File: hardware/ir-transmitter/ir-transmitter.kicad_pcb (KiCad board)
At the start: 2 copper layers, 50 x 20 mm, 16 parts, among them T1 Q_NMOS_GSD, T2 Q_NMOS_GSD, X1 Conn_01x05

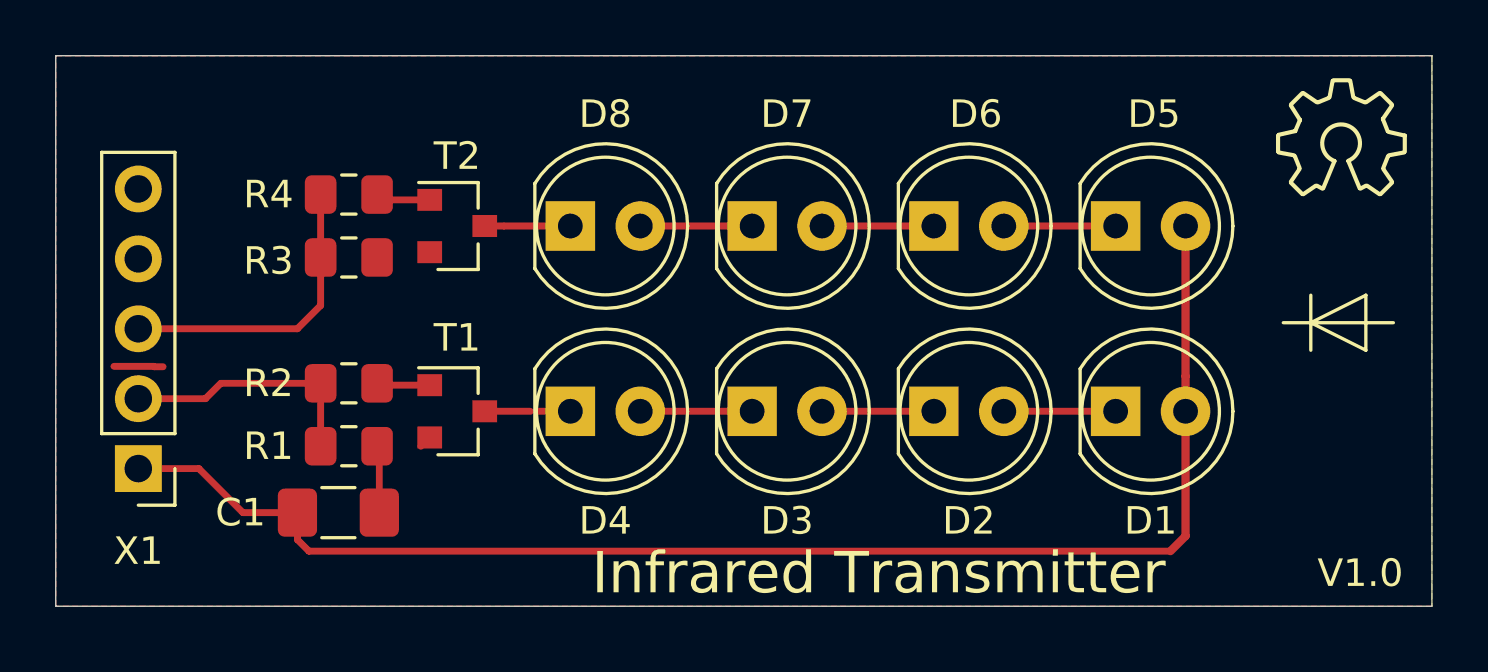
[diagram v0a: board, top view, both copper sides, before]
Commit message: Make receiver PCB two-sided
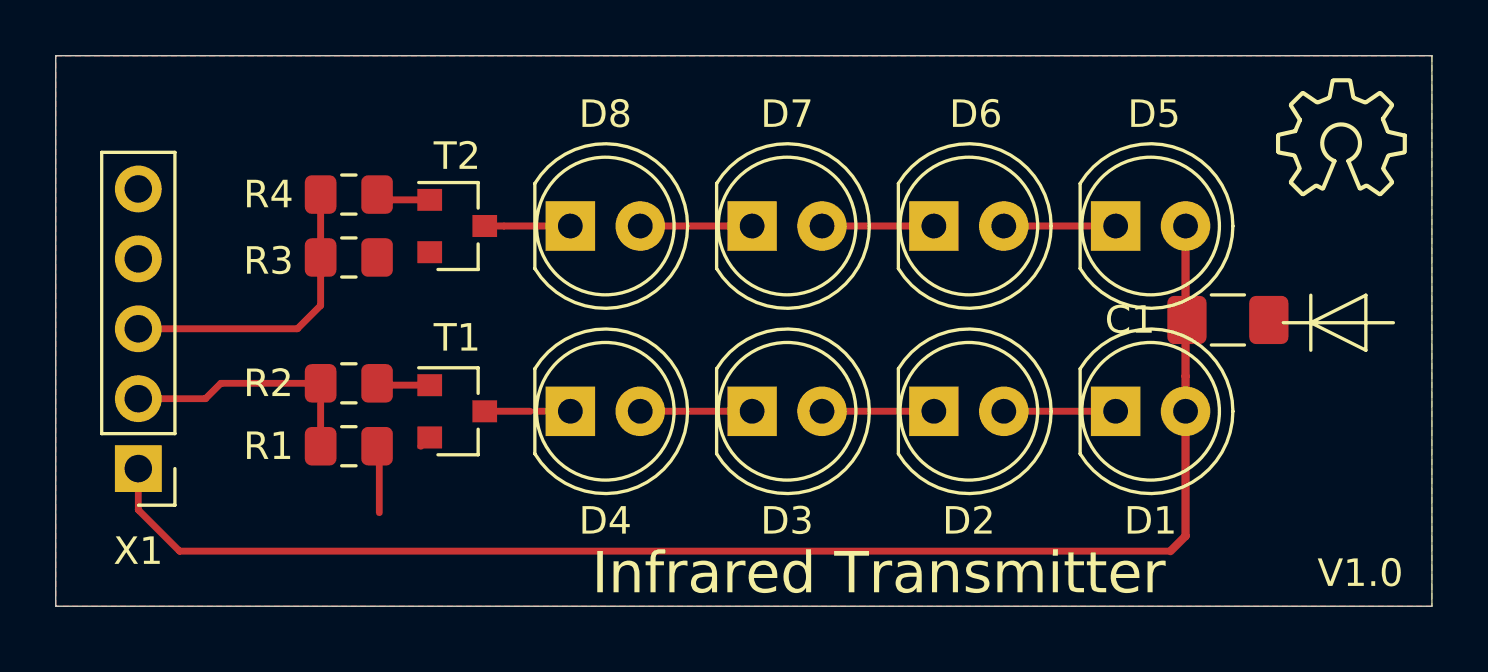
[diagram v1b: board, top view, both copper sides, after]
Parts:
- moved C1 33.1 mm to (122.6, 139.6)
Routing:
- net (no net): track 1.79 -> 0.00 mm

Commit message: Double-sided PCBs
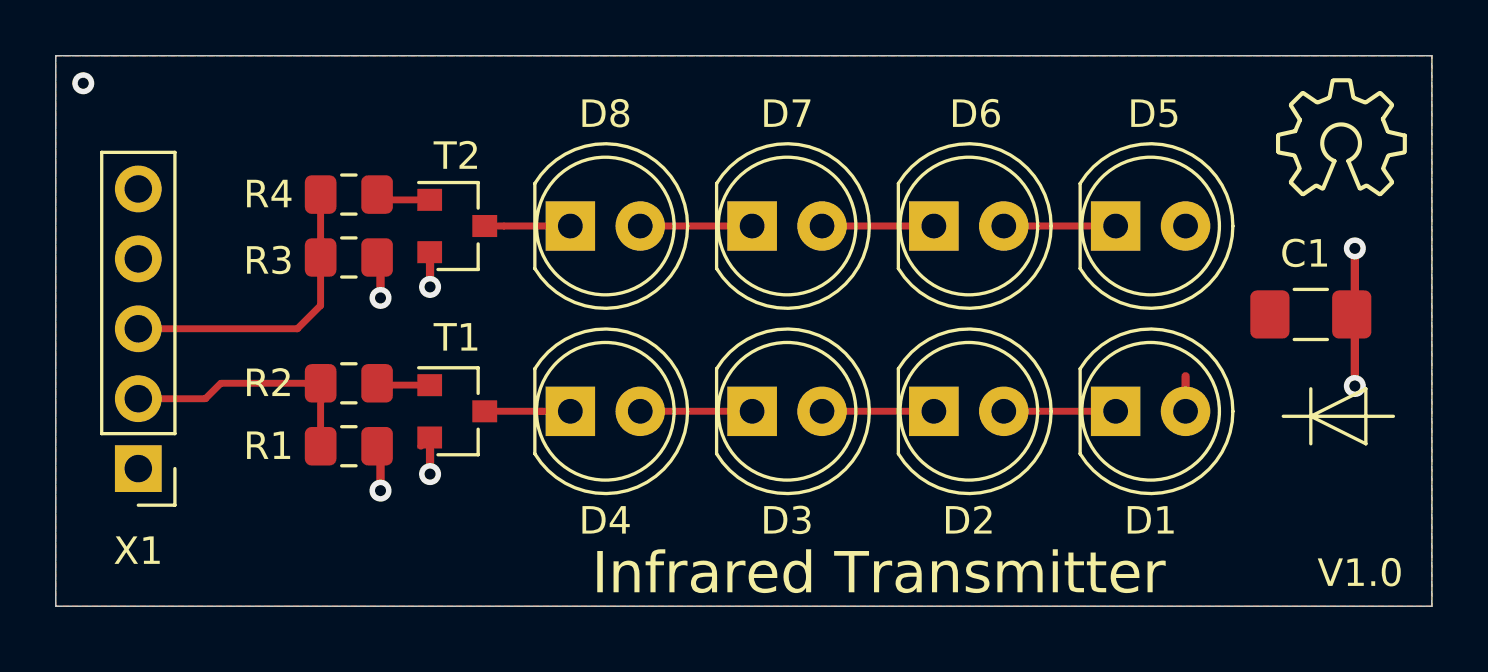
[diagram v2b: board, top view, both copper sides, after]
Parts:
- moved C1 3.02 mm to (125.6, 139.4)
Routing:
- net +5V: track 51.7 -> 1.27 mm
- net GND: track 3.17 -> 11.1 mm, vias 0 -> 7
- added copper zone on F.Cu, net +5V
- added copper zone on B.Cu, net GND
- removed copper zone on F.Cu, net GND
